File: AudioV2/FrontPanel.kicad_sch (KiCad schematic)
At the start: 31 parts, among them SW402 Cosland 2MS1 PWR, SW501 Cosland 2MD1 DEST, U1609 XC8107AC20MR-G, U1610 MCP23017 (UI 0x22)

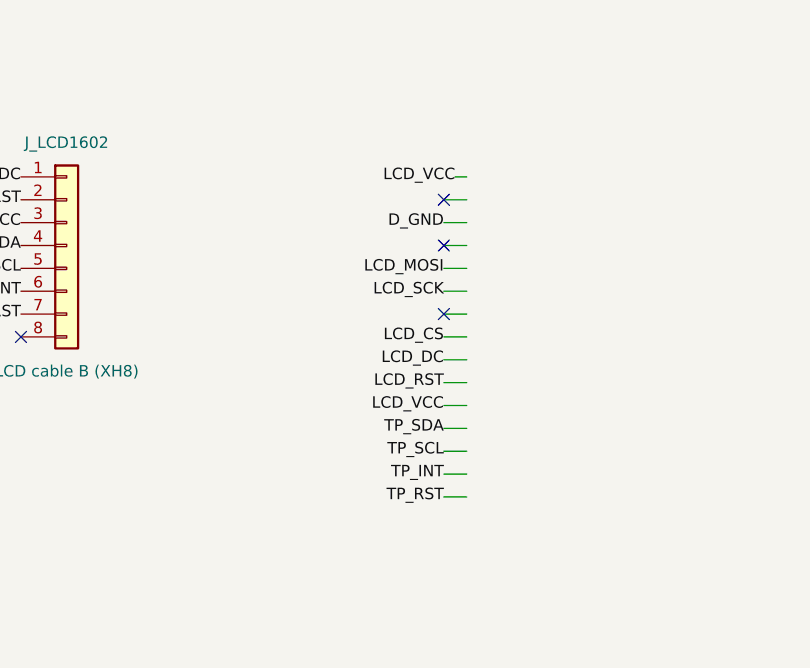
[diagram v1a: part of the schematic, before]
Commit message: AudioV2: 娘基板（Switch/Relay）の AMP_SEL 配線・デカップを音質優先で追い込む (#42)
- Switch: AMP_SEL を1ホップずつ B.Cu へ、TMUX の南北 D を本体下で直結、TMUX に 1 µF（0603）追加・100 nF を足元の裏へ、J_ANA301 の L/R 交差を 90° に
- Relay: リレー列↔ドライバ間の帯を組み直し（コイル線・L バス・ドライバ 100 nF・+5V_COIL 近道）、AMP_SEL の L/R を別の通り道に分離（2 mm 以内並走 L↔R 18 → 0 mm）
- 共通: MCP23017 の 100 nF を 0603 で VDD/VSS の足の真上へ
- ルートを手編集所有に切替、ERC 残骸の片付け（59 → 5）、期待値と PARTS.md を実測に合わせる

DRC 新規違反 0・未接続不変・schematic parity 0。ERC 5。部品 355。

Co-Authored-By: Claude Opus 5.5 <noreply@anthropic.com>
Claude-Session: https://claude.ai/code/session_01NpwAm89hZpJTCZphnQ6odp
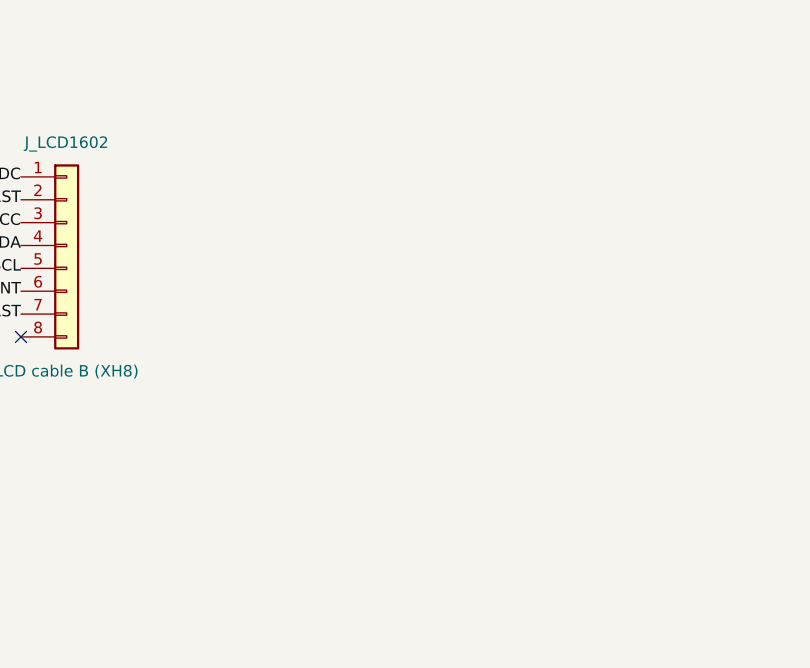
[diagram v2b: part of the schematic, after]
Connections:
- no-connect marks 28 -> 25
